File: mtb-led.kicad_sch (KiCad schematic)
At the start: 57 parts, among them J7 AVR-ISP-6, J9 DEBUG, SW1 SW_Push, U1 ATmega328PB-A, U2 78M05, U3 TLC5940PWP, U4 TLC5940PWP, U5 MAX487E, Y1 14.7456 MHz

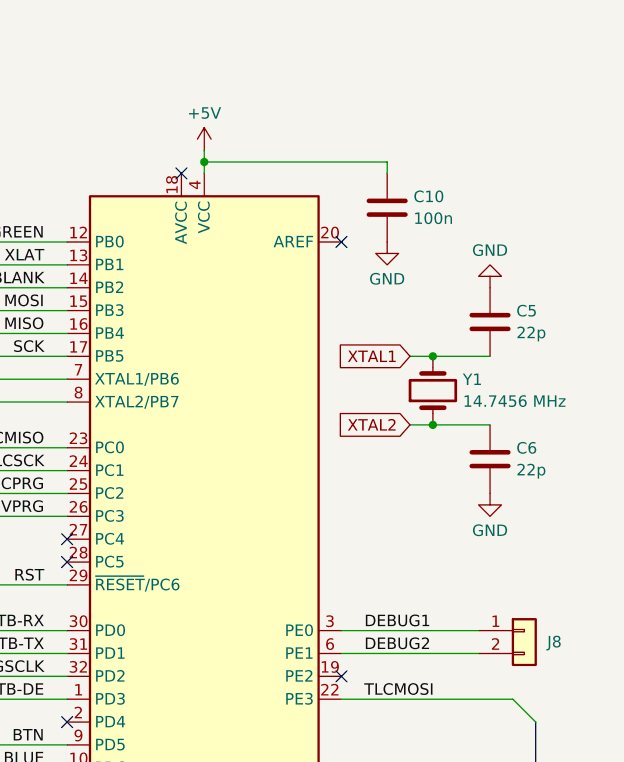
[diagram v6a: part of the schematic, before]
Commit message: Add AREF 100nF capacitor.
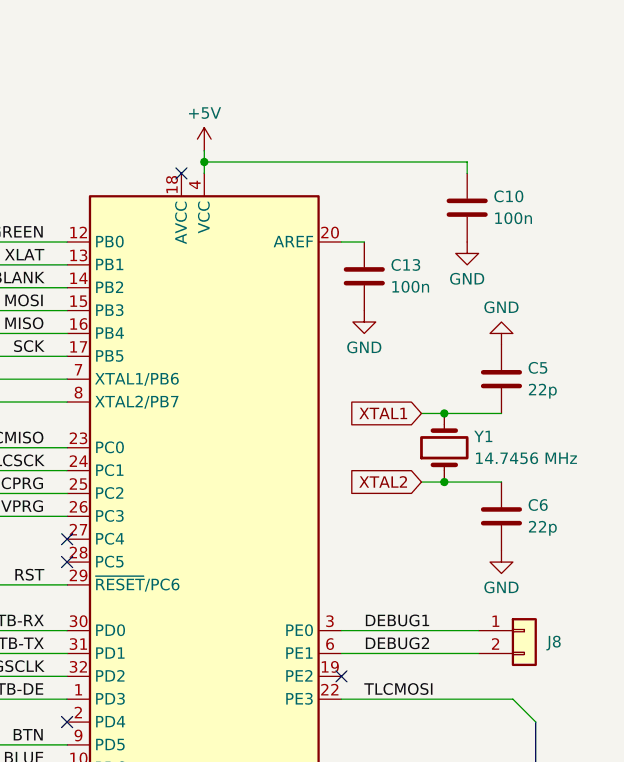
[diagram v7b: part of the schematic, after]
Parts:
- added C13: 100n, Capacitor_SMD:C_0805_2012Metric, symbol Device:C
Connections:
- net GND: now also C13.2
- net at U1.20 (AREF): now also C13.1
- no-connect marks 8 -> 7
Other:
- moved on the sheet: C10, C5, C6, Y1

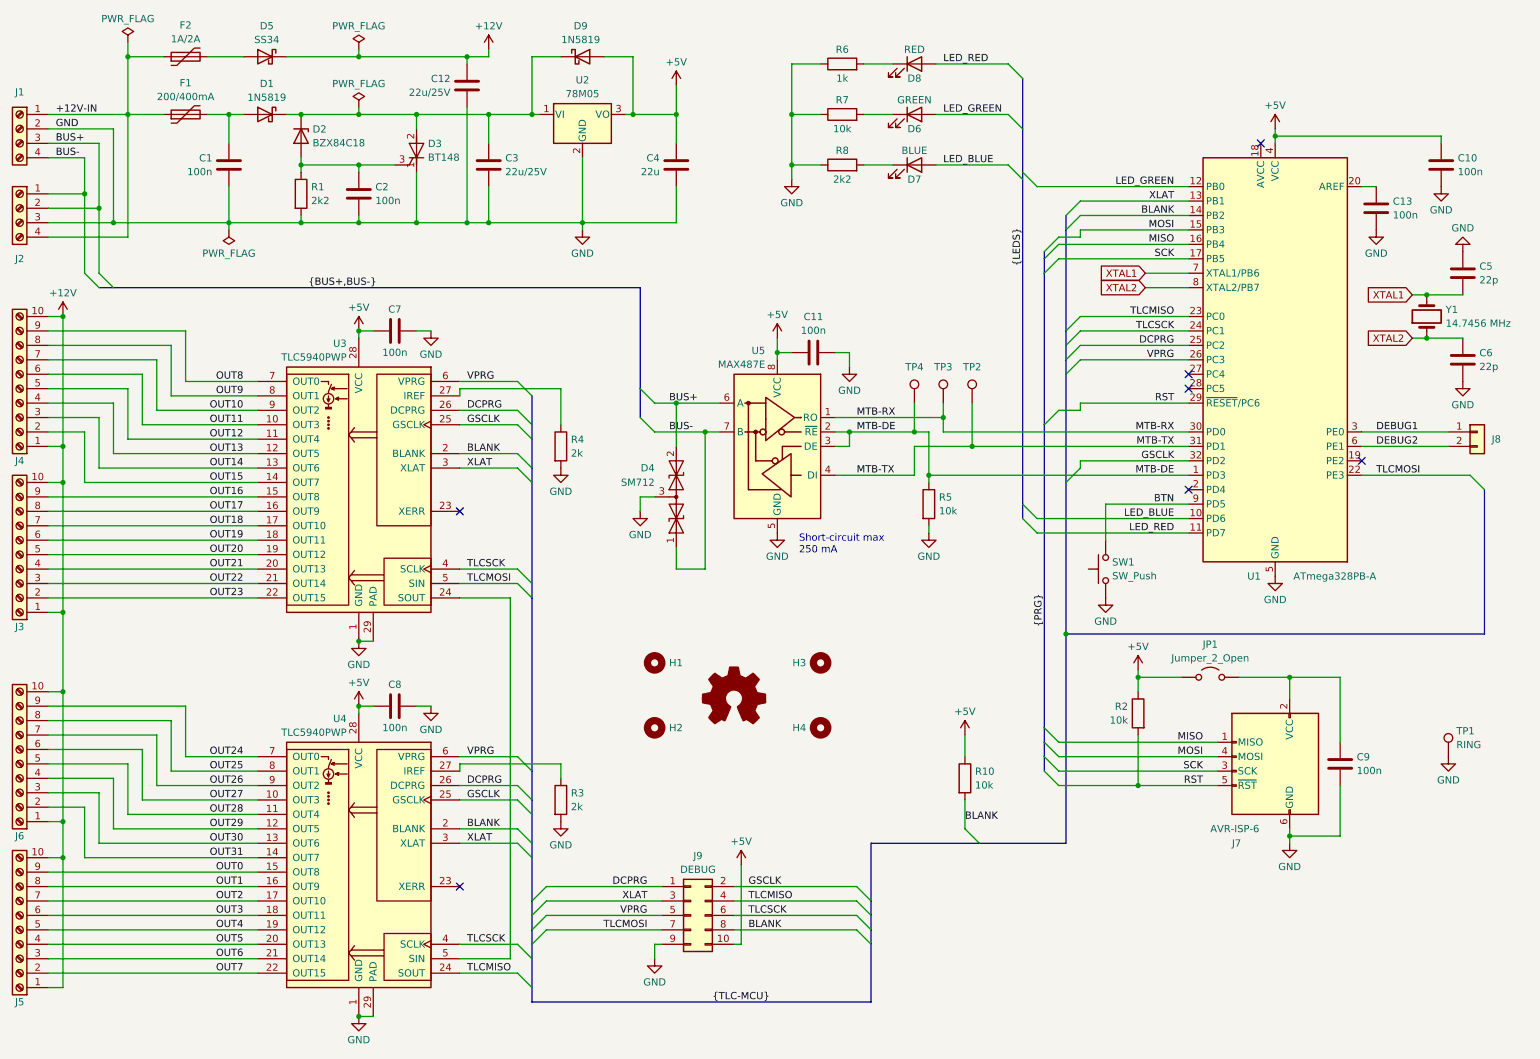
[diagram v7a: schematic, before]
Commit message: Remove DCPG & VPRG signals MCU <-> TLC.
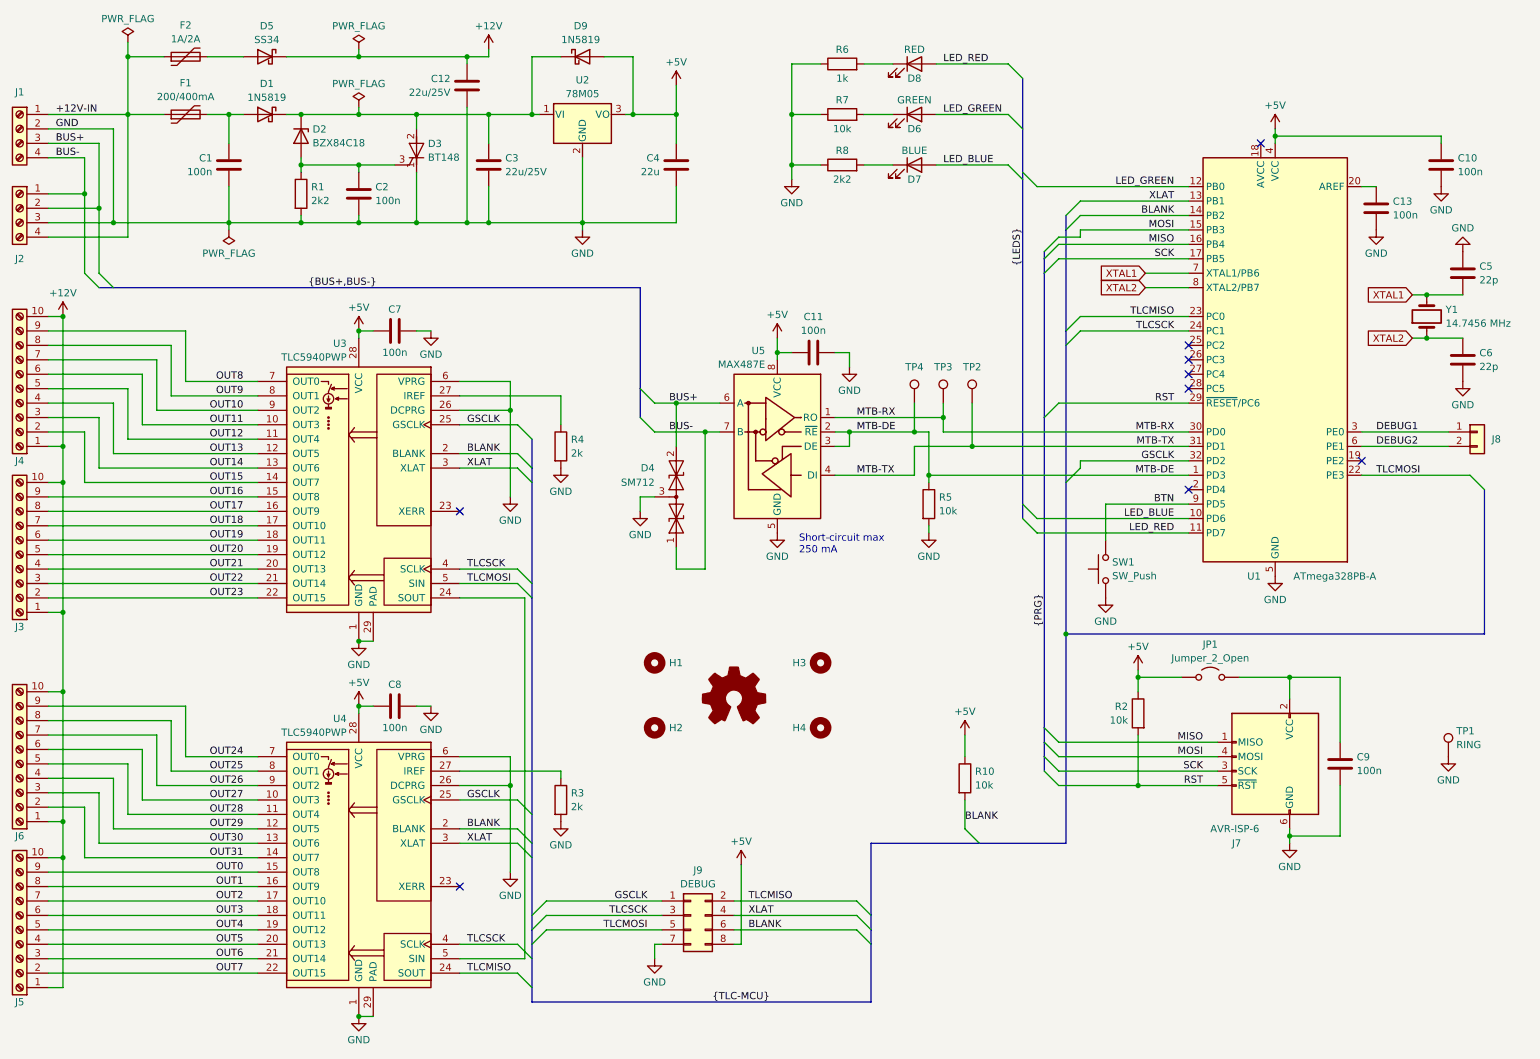
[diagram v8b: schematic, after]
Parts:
- J9: footprint Connector_PinHeader_2.54mm:PinHeader_2x05_P2.54mm_Vertical -> Connector_PinHeader_2.54mm:PinHeader_2x04_P2.54mm_Vertical; symbol Connector_Generic:Conn_02x05_Odd_Even -> Connector_Generic:Conn_02x04_Odd_Even
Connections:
- net +5V: now also J9.8 (Pin_8); no longer J9.10 (Pin_10)
- net BLANK: now also J9.6 (Pin_6); no longer J9.8 (Pin_8)
- net GND: now also J9.7 (Pin_7), U3.26 (DCPRG), U3.6 (VPRG), U4.26 (DCPRG), U4.6 (VPRG); no longer J9.9 (Pin_9)
- net GSCLK: now also J9.1 (Pin_1); no longer J9.2 (Pin_2)
- net TLCMISO: now also J9.2 (Pin_2); no longer J9.4 (Pin_4)
- net TLCMOSI: now also J9.5 (Pin_5); no longer J9.7 (Pin_7)
- net TLCSCK: now also J9.3 (Pin_3); no longer J9.6 (Pin_6)
- net XLAT: now also J9.4 (Pin_4); no longer J9.3 (Pin_3)
- removed net DCPRG: J9.1 (Pin_1), U1.25 (PC2), U3.26 (DCPRG), U4.26 (DCPRG)
- removed net VPRG: J9.5 (Pin_5), U1.26 (PC3), U3.6 (VPRG), U4.6 (VPRG)
- no-connect marks 7 -> 9
